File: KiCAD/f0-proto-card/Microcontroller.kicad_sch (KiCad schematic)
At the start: 25 parts, among them J7 ORESAT-DEBUG-CONNECTOR-ALL, U1 TCAN330, U7 STM32F091C, X2 CRYSTAL-WITH-GND

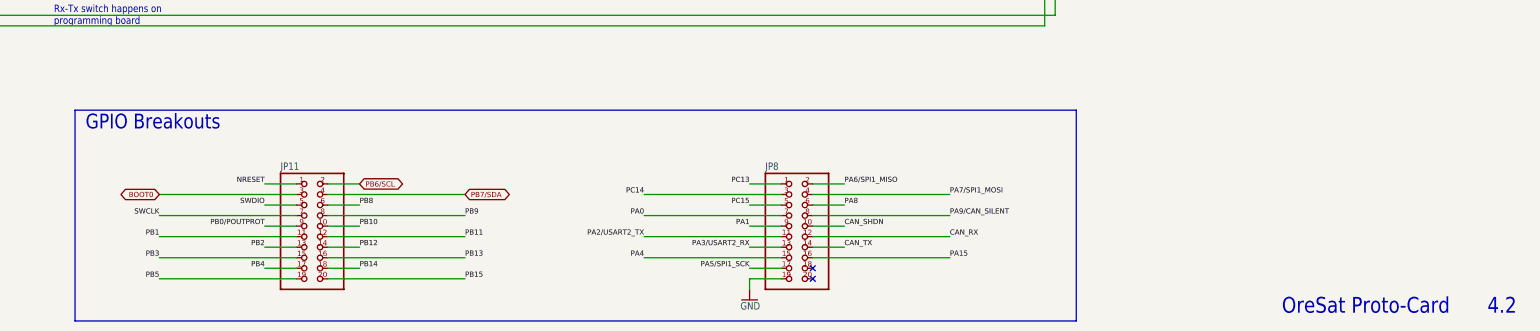
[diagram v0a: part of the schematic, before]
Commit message: Some design review changes for protocard v5.0
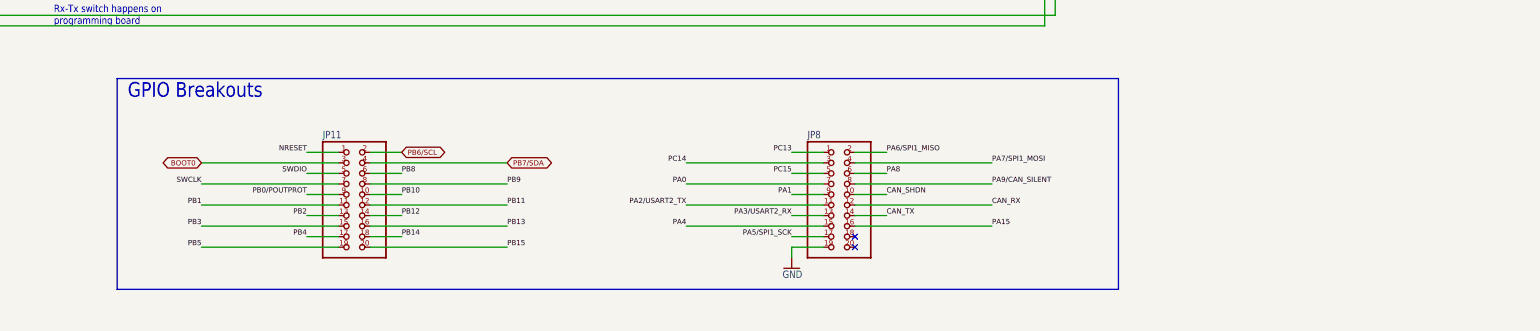
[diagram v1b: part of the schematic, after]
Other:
- note removed: "4.2"
- note removed: "OreSat Proto-Card"
- title: (none) -> oresat-proto-card
- moved on the sheet: JP11, JP8

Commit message: Finished cleaning up protocard
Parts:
- C13, C14, C15, C18, C19, C20, C21, R47, R48, R49, R50, R51: footprint oresat-proto-card:.0603-C-NOSILK -> oresat-passives:0603-C-NOSILK
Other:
- moved on the sheet: R49, TP26, TP27, TP28, TP29, TP30
